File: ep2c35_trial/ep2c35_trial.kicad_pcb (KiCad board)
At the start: 4 copper layers, 70.4 x 57.6 mm, 144 parts, among them J1 Conn_02x21_Odd_Even, J2 Conn_02x21_Odd_Even, J3 3M_8540-4500PL, J4 USB3_B_Micro_Amphenol_GSB343K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, J5 Conn_02x05_Odd_Even, J6 Conn_01x02_Male, J7 Conn_01x02_Male, J8 Conn_01x02_Male, J9 Conn_01x02_Male, U1 EP2C5F484, U2 MIC37302, U3 FT600Q-B-T, U4 W25Q16JVSNIQ, U5 MIC39102, U6 MIC49150-1.2, X1 FNETHE025, Y1 ABM7-30.000MHZ-D2Y-T

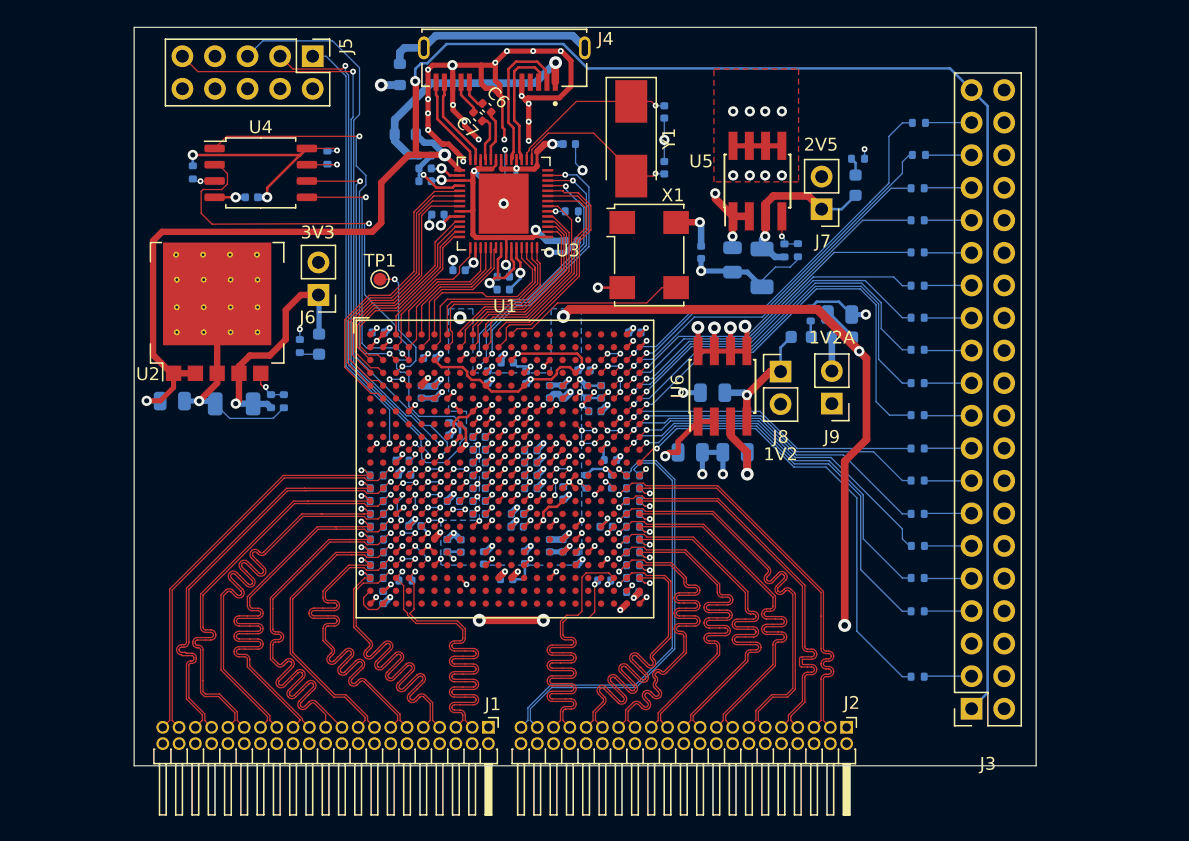
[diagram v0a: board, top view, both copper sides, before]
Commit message: Add lvds_tx.
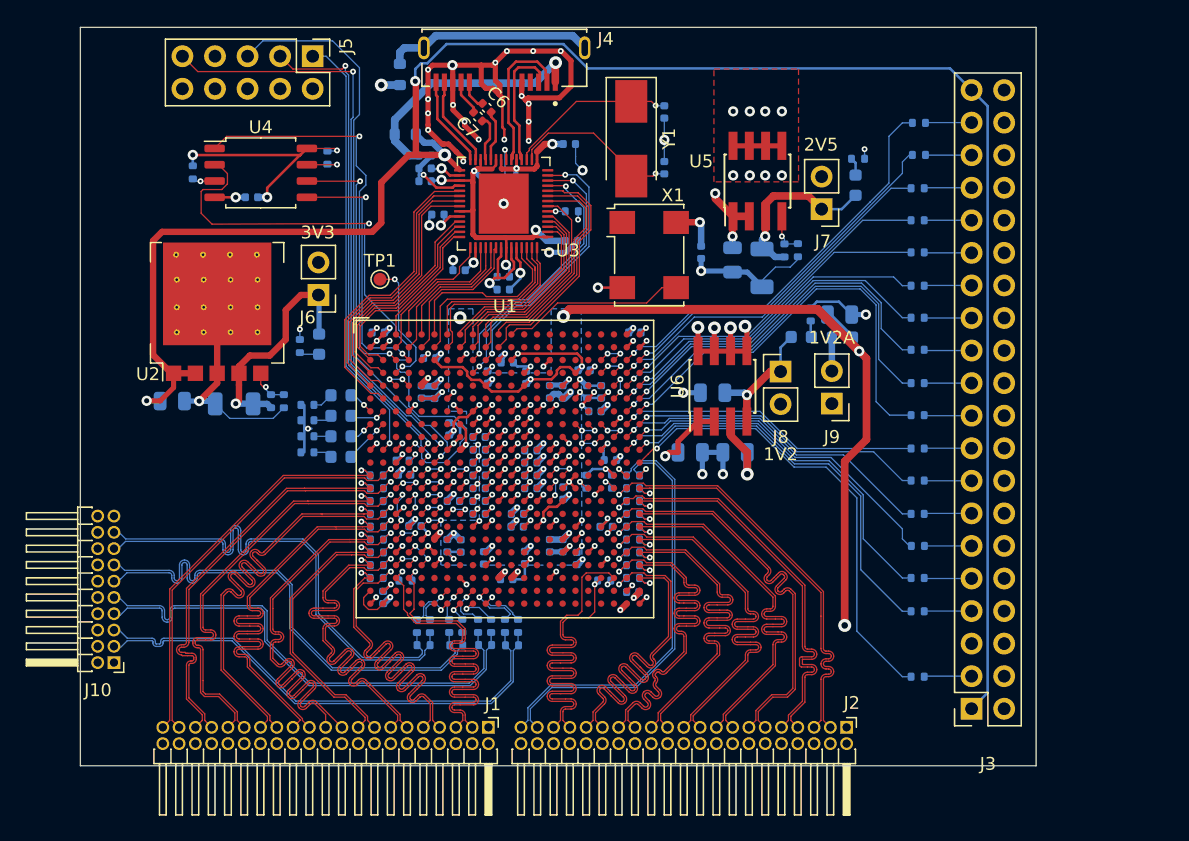
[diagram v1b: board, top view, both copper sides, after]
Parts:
- added D4: LED, LED_SMD:LED_0603_1608Metric, B.Cu at (131.7, 75.8)
- added D5: LED, LED_SMD:LED_0603_1608Metric, B.Cu at (131.7, 77.3)
- added D6: LED, LED_SMD:LED_0603_1608Metric, B.Cu at (131.7, 79.0)
- added D7: LED, LED_SMD:LED_0603_1608Metric, B.Cu at (131.7, 80.5)
- added J10: Conn_02x10_Odd_Even, Connector_PinHeader_1.27mm:PinHeader_2x10_P1.27mm_Horizontal, F.Cu at (114.0, 96.6)
- added R52: 1k, Resistor_SMD:R_0402_1005Metric, B.Cu at (129.1, 76.5)
- added R53: 1k, Resistor_SMD:R_0402_1005Metric, B.Cu at (129.1, 77.7)
- added R54: 1k, Resistor_SMD:R_0402_1005Metric, B.Cu at (129.1, 79.0)
- added R55: 1k, Resistor_SMD:R_0402_1005Metric, B.Cu at (129.1, 80.2)
- added R56: 120, Resistor_SMD:R_0402_1005Metric, B.Cu at (144.5, 93.7)
- added R57: 170, Resistor_SMD:R_0402_1005Metric, B.Cu at (145.1, 95.2)
- added R58: 120, Resistor_SMD:R_0402_1005Metric, B.Cu at (145.5, 93.7)
- added R59: 120, Resistor_SMD:R_0402_1005Metric, B.Cu at (142.4, 93.7)
- added R60: 170, Resistor_SMD:R_0402_1005Metric, B.Cu at (142.9, 95.2)
- added R61: 120, Resistor_SMD:R_0402_1005Metric, B.Cu at (143.4, 93.7)
- added R62: 120, Resistor_SMD:R_0402_1005Metric, B.Cu at (140.2, 93.7)
- added R63: 170, Resistor_SMD:R_0402_1005Metric, B.Cu at (140.7, 95.2)
- added R64: 120, Resistor_SMD:R_0402_1005Metric, B.Cu at (141.2, 93.7)
- added R65: 120, Resistor_SMD:R_0402_1005Metric, B.Cu at (137.6, 93.8)
- added R66: 170, Resistor_SMD:R_0402_1005Metric, B.Cu at (138.2, 95.2)
- added R67: 120, Resistor_SMD:R_0402_1005Metric, B.Cu at (138.7, 93.8)
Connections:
- U1 pad AA10: unconnected-(U1-PadAA10) -> /LVDS_TX_DATA0_RAW_N
- U1 pad AA7: unconnected-(U1-PadAA7) -> /LVDS_TX_DATA3_RAW_N
- U1 pad AA8: unconnected-(U1-PadAA8) -> /LVDS_TX_DATA2_RAW_N
- U1 pad AA9: unconnected-(U1-PadAA9) -> /LVDS_TX_DATA1_RAW_N
- U1 pad AB10: unconnected-(U1-PadAB10) -> /LVDS_TX_DATA0_RAW_P
- U1 pad AB7: unconnected-(U1-PadAB7) -> /LVDS_TX_DATA3_RAW_P
- U1 pad AB8: unconnected-(U1-PadAB8) -> /LVDS_TX_DATA2_RAW_P
- U1 pad AB9: unconnected-(U1-PadAB9) -> /LVDS_TX_DATA1_RAW_P
- U1 pad G1: unconnected-(U1-PadG1) -> /LED0
- U1 pad G2: unconnected-(U1-PadG2) -> /LED1
- U1 pad H1: unconnected-(U1-PadH1) -> /LED2
- U1 pad H2: unconnected-(U1-PadH2) -> /LED3
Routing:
- net /LVDS_TX_DATA0_P: track 0.00 -> 38.7 mm
- net /LVDS_TX_DATA0_N: track 0.00 -> 38.4 mm
- net /LVDS_TX_DATA1_P: track 0.00 -> 38.4 mm
- net /LVDS_TX_DATA2_P: track 0.00 -> 38.3 mm
- net /LVDS_TX_DATA3_P: track 0.00 -> 38.2 mm
- net /LVDS_TX_DATA1_N: track 0.00 -> 38.1 mm
- net /LVDS_TX_DATA3_N: track 0.00 -> 37.9 mm
- net /LVDS_TX_DATA2_N: track 0.00 -> 37.9 mm
- net +1V2A: track 66.1 -> 61.1 mm, vias 10 -> 8
- net /LVDS_TX_DATA0_RAW_N: track 0.00 -> 4.28 mm, vias 0 -> 1
- net GND: track 232.5 -> 236.8 mm, vias 126 -> 127
- net /LVDS_TX_DATA0_RAW_P: track 0.00 -> 4.20 mm, vias 0 -> 1
- net /LVDS_TX_DATA3_RAW_N: track 0.00 -> 3.70 mm, vias 0 -> 1
- net /LVDS_TX_DATA1_RAW_N: track 0.00 -> 3.60 mm, vias 0 -> 1
- net /LED3: track 0.00 -> 3.59 mm, vias 0 -> 1
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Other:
- board size 70.4 x 57.6 mm -> 74.5 x 57.6 mm

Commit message: Top ground plan.
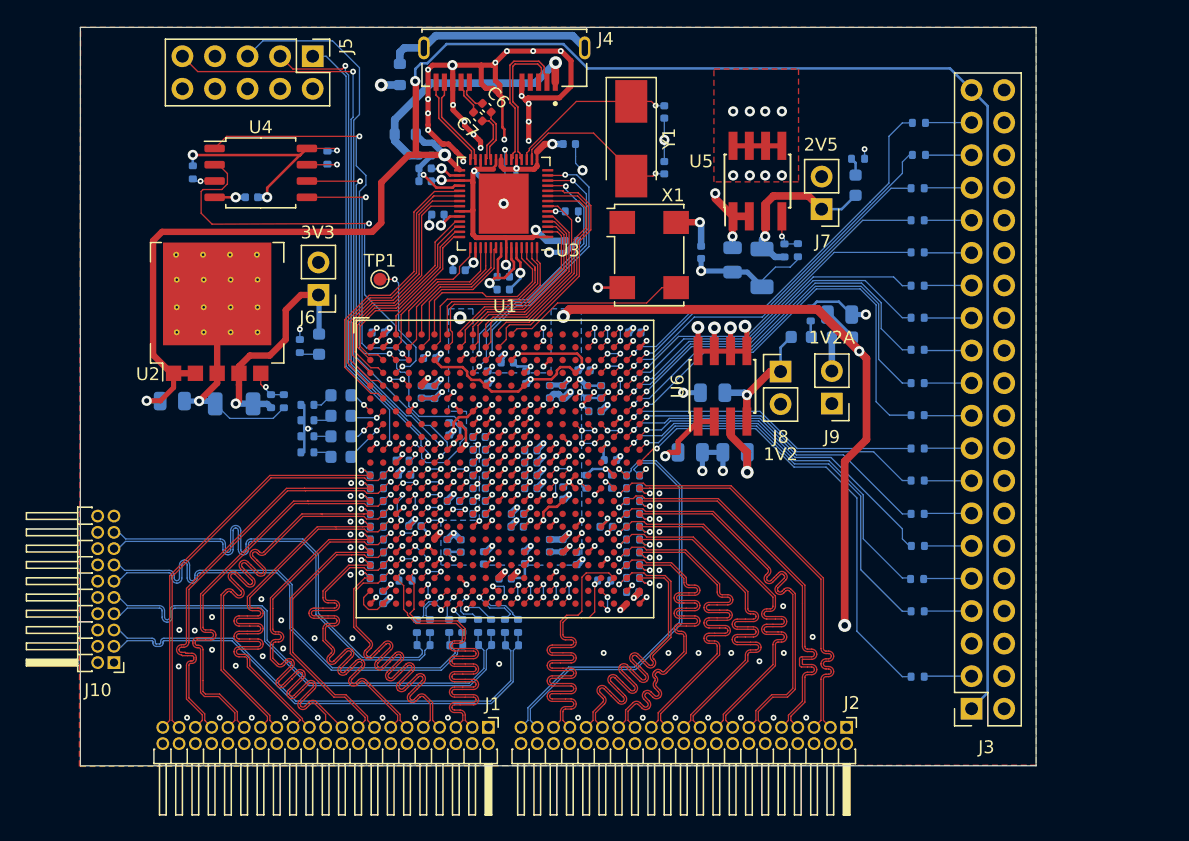
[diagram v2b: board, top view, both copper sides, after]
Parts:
- moved C69 0.12 mm to (144.5, 90.0)
- moved R34 0.09 mm to (176.7, 90.1)
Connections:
- C1 pad 2: GND -> GNDD
- C10 pad 1: GND -> GNDD
- C11 pad 1: GND -> GNDD
- C12 pad 1: GND -> GNDD
- C13 pad 1: GND -> GNDD
- C14 pad 1: GND -> GNDD
- C15 pad 1: GND -> GNDD
- C16 pad 1: GND -> GNDD
- C17 pad 1: GND -> GNDD
- C18 pad 1: GND -> GNDD
- C19 pad 1: GND -> GNDD
- C2 pad 2: GND -> GNDD
- C20 pad 1: GND -> GNDD
- C22 pad 1: GND -> GNDD
- C23 pad 1: GND -> GNDD
- C24 pad 1: GND -> GNDD
- C25 pad 1: GND -> GNDD
- C26 pad 1: GND -> GNDD
- C27 pad 1: GND -> GNDD
- C28 pad 1: GND -> GNDD
- C29 pad 1: GND -> GNDD
- C3 pad 2: GND -> GNDD
- C30 pad 1: GND -> GNDD
- C31 pad 2: GND -> GNDD
- C32 pad 2: GND -> GNDD
- C33 pad 2: GND -> GNDD
- C34 pad 2: GND -> GNDD
- C35 pad 2: GND -> GNDD
- C36 pad 2: GND -> GNDD
- C37 pad 2: GND -> GNDD
- C38 pad 2: GND -> GNDD
- C39 pad 2: GND -> GNDD
- C4 pad 2: GND -> GNDD
- C40 pad 2: GND -> GNDD
- C41 pad 2: GND -> GNDD
- C42 pad 2: GND -> GNDD
- C43 pad 2: GND -> GNDD
- C44 pad 2: GND -> GNDD
- C45 pad 2: GND -> GNDD
- C46 pad 2: GND -> GNDD
- C47 pad 2: GND -> GNDD
- C48 pad 2: GND -> GNDD
- C49 pad 2: GND -> GNDD
- C5 pad 2: GND -> GNDD
- C50 pad 2: GND -> GNDD
- C51 pad 2: GND -> GNDD
- C52 pad 2: GND -> GNDD
- C53 pad 2: GND -> GNDD
- C54 pad 2: GND -> GNDD
- C55 pad 2: GND -> GNDD
- C56 pad 2: GND -> GNDD
- C57 pad 2: GND -> GNDD
- C58 pad 2: GND -> GNDD
- C59 pad 2: GND -> GNDD
- C60 pad 2: GND -> GNDD
- C61 pad 2: GND -> GNDD
- C62 pad 2: GND -> GNDD
- C63 pad 2: GND -> GNDD
- C64 pad 2: GND -> GNDD
- C65 pad 2: GND -> GNDD
- C66 pad 2: GND -> GNDD
- C67 pad 2: GND -> GNDD
- C68 pad 2: GND -> GNDD
- C69 pad 2: GND -> GNDD
- C70 pad 2: GND -> GNDD
- C8 pad 1: GND -> GNDD
- C9 pad 1: GND -> GNDD
- FB2 pad 2: GND -> GNDD
- J1 pad 1: GND -> GNDD
- J1 pad 10: GND -> GNDD
- J1 pad 12: GND -> GNDD
- J1 pad 14: GND -> GNDD
- J1 pad 16: GND -> GNDD
- J1 pad 18: GND -> GNDD
- J1 pad 2: GND -> GNDD
- J1 pad 20: GND -> GNDD
- J1 pad 22: GND -> GNDD
- J1 pad 24: GND -> GNDD
- J1 pad 26: GND -> GNDD
- J1 pad 28: GND -> GNDD
- J1 pad 30: GND -> GNDD
- J1 pad 32: GND -> GNDD
- J1 pad 34: GND -> GNDD
- J1 pad 36: GND -> GNDD
- J1 pad 38: GND -> GNDD
- J1 pad 4: GND -> GNDD
- J1 pad 40: GND -> GNDD
- J1 pad 42: GND -> GNDD
- J1 pad 6: GND -> GNDD
- J1 pad 8: GND -> GNDD
- J10 pad 1: GND -> GNDD
- J10 pad 10: GND -> GNDD
- J10 pad 12: GND -> GNDD
- J10 pad 14: GND -> GNDD
- J10 pad 16: GND -> GNDD
- J10 pad 18: GND -> GNDD
- J10 pad 19: GND -> GNDD
- J10 pad 2: GND -> GNDD
- J10 pad 20: GND -> GNDD
- J10 pad 4: GND -> GNDD
- J10 pad 5: /LVDS_TX_DATA0_N -> GNDD
- J10 pad 6: GND -> GNDD
- J10 pad 8: GND -> GNDD
- J2 pad 1: GND -> GNDD
- J2 pad 10: GND -> GNDD
- J2 pad 12: GND -> GNDD
- J2 pad 14: GND -> GNDD
- J2 pad 16: GND -> GNDD
- J2 pad 18: GND -> GNDD
- J2 pad 2: GND -> GNDD
- J2 pad 20: GND -> GNDD
- J2 pad 22: GND -> GNDD
- J2 pad 24: GND -> GNDD
- J2 pad 26: GND -> GNDD
- J2 pad 28: GND -> GNDD
- J2 pad 30: GND -> GNDD
- J2 pad 32: GND -> GNDD
- J2 pad 34: GND -> GNDD
- J2 pad 36: GND -> GNDD
- J2 pad 38: GND -> GNDD
- J2 pad 4: GND -> GNDD
- J2 pad 40: GND -> GNDD
- J2 pad 42: GND -> GNDD
- J2 pad 6: GND -> GNDD
- J2 pad 8: GND -> GNDD
- J3 pad 10: GND -> GNDD
- J3 pad 12: GND -> GNDD
- J3 pad 14: GND -> GNDD
- J3 pad 16: GND -> GNDD
- J3 pad 18: GND -> GNDD
- J3 pad 2: GND -> GNDD
- J3 pad 20: GND -> GNDD
- J3 pad 22: GND -> GNDD
- J3 pad 24: GND -> GNDD
- J3 pad 26: GND -> GNDD
- J3 pad 28: GND -> GNDD
- J3 pad 30: GND -> GNDD
- J3 pad 32: GND -> GNDD
- J3 pad 34: GND -> GNDD
- J3 pad 36: GND -> GNDD
- J3 pad 38: GND -> GNDD
- J3 pad 4: GND -> GNDD
- J3 pad 40: GND -> GNDD
- J3 pad 6: GND -> GNDD
- J3 pad 8: GND -> GNDD
- J4 pad 5: GND -> GNDD
- J4 pad 8: GND -> GNDD
- J5 pad 10: GND -> GNDD
- J5 pad 2: GND -> GNDD
- R1 pad 2: GND -> GNDD
- R31 pad 1: GND -> GNDD
- R49 pad 1: GND -> GNDD
- R50 pad 1: GND -> GNDD
- R51 pad 1: GND -> GNDD
- R52 pad 1: GND -> GNDD
- R53 pad 1: GND -> GNDD
- R54 pad 1: GND -> GNDD
- R55 pad 1: GND -> GNDD
- R56 pad 1: /LVDS_TX_DATA0_N -> GNDD
- R57 pad 2: /LVDS_TX_DATA0_N -> GNDD
- R9 pad 1: GND -> GNDD
- U1 pad A1: GND -> GNDD
- U1 pad A14: unconnected-(U1-PadA14) -> /LVDS76
- U1 pad A18: unconnected-(U1-PadA18) -> /LVDS96
- U1 pad A19: unconnected-(U1-PadA19) -> /LVDS97
- U1 pad A20: unconnected-(U1-PadA20) -> /LVDS98
- U1 pad A22: GND -> GNDD
- U1 pad AA11: unconnected-(U1-PadAA11) -> /LVDS177
- U1 pad AA12: unconnected-(U1-PadAA12) -> /LVDS176
- U1 pad AA13: unconnected-(U1-PadAA13) -> /LVDS174
- U1 pad AA14: unconnected-(U1-PadAA14) -> /LVDS170
- U1 pad AA15: unconnected-(U1-PadAA15) -> /LVDS169
- U1 pad AA16: unconnected-(U1-PadAA16) -> /LVDS168
- U1 pad AA19: unconnected-(U1-PadAA19) -> /LVDS152
- U1 pad AA2: GND -> GNDD
- U1 pad AA21: GND -> GNDD
- U1 pad AA5: unconnected-(U1-PadAA5) -> /LVDS197
- U1 pad AB1: GND -> GNDD
- U1 pad AB11: unconnected-(U1-PadAB11) -> /LVDS177
- U1 pad AB12: unconnected-(U1-PadAB12) -> /LVDS176
- U1 pad AB13: unconnected-(U1-PadAB13) -> /LVDS174
- U1 pad AB14: unconnected-(U1-PadAB14) -> /LVDS170
- U1 pad AB15: unconnected-(U1-PadAB15) -> /LVDS169
- U1 pad AB16: unconnected-(U1-PadAB16) -> /LVDS168
- U1 pad AB19: unconnected-(U1-PadAB19) -> /LVDS152
- U1 pad AB22: GND -> GNDD
- U1 pad AB5: unconnected-(U1-PadAB5) -> /LVDS197
- U1 pad B14: unconnected-(U1-PadB14) -> /LVDS76
- U1 pad B18: unconnected-(U1-PadB18) -> /LVDS96
- U1 pad B19: unconnected-(U1-PadB19) -> /LVDS97
- U1 pad B2: GND -> GNDD
- U1 pad B20: unconnected-(U1-PadB20) -> /LVDS98
- U1 pad B21: GND -> GNDD
- U1 pad C15: GND -> GNDD
- U1 pad C5: GND -> GNDD
- U1 pad C8: GND -> GNDD
- U1 pad D10: GND -> GNDD
- U1 pad D13: GND -> GNDD
- U1 pad D18: GND -> GNDD
- U1 pad E16: GND -> GNDD
- U1 pad E17: GND -> GNDD
- U1 pad F18: GND -> GNDD
- U1 pad F19: GND -> GNDD
- U1 pad F5: GND -> GNDD
- U1 pad F6: GND -> GNDD
- U1 pad F7: GND -> GNDD
- U1 pad G10: GND -> GNDD
- U1 pad G13: GND -> GNDD
- U1 pad G15: GND -> GNDD
- U1 pad G4: GND -> GNDD
- U1 pad H10: GND -> GNDD
- U1 pad H20: GND -> GNDD
- U1 pad H9: GND -> GNDD
- U1 pad J8: GND -> GNDD
- U1 pad J9: GND -> GNDD
- U1 pad K1: GND -> GNDD
- U1 pad K10: GND -> GNDD
- U1 pad K11: GND -> GNDD
- U1 pad K12: GND -> GNDD
- U1 pad K13: GND -> GNDD
- U1 pad K15: GND -> GNDD
- U1 pad K16: GND -> GNDD
- U1 pad K19: GND -> GNDD
- U1 pad K3: GND -> GNDD
- U1 pad K7: GND -> GNDD
- U1 pad L10: GND -> GNDD
- U1 pad L11: GND -> GNDD
- U1 pad L12: GND -> GNDD
- U1 pad L13: GND -> GNDD
- U1 pad L15: GND -> GNDD
- U1 pad M10: GND -> GNDD
- U1 pad M11: GND -> GNDD
- U1 pad M12: GND -> GNDD
- U1 pad M13: GND -> GNDD
- U1 pad M17: GND -> GNDD
- U1 pad M4: GND -> GNDD
- U1 pad N10: GND -> GNDD
- U1 pad N11: GND -> GNDD
- U1 pad N12: GND -> GNDD
- U1 pad N13: GND -> GNDD
- U1 pad N16: GND -> GNDD
- U1 pad N17: GND -> GNDD
- U1 pad N19: GND -> GNDD
- U1 pad N7: GND -> GNDD
- U1 pad N8: GND -> GNDD
- U1 pad P8: GND -> GNDD
- U1 pad P9: GND -> GNDD
- U1 pad R13: GND -> GNDD
- U1 pad R3: GND -> GNDD
- U1 pad R9: GND -> GNDD
- U1 pad T10: GND -> GNDD
- U1 pad T13: GND -> GNDD
- U1 pad T17: GND -> GNDD
- U1 pad T20: GND -> GNDD
- U1 pad U5: GND -> GNDD
- U1 pad V16: GND -> GNDD
- U1 pad V17: GND -> GNDD
- U1 pad V18: GND -> GNDD
- U1 pad V3: GND -> GNDD
- U1 pad V5: GND -> GNDD
- U1 pad V6: GND -> GNDD
- U1 pad V7: GND -> GNDD
- U1 pad W10: GND -> GNDD
- U1 pad W13: GND -> GNDD
- U1 pad W19: GND -> GNDD
- U1 pad Y15: GND -> GNDD
- U1 pad Y5: unconnected-(U1-PadY5) -> /LVDS198
- U1 pad Y6: unconnected-(U1-PadY6) -> /LVDS198
- U1 pad Y8: GND -> GNDD
- U2 pad 3: GND -> GNDD
- U3 pad 32: GND -> GNDD
- U3 pad 49: GND -> GNDD
- U3 pad 51: GND -> GNDD
- U3 pad 57: GND -> GNDD
- U4 pad 4: GND -> GNDD
- U5 pad 5: GND -> GNDD
- U5 pad 6: GND -> GNDD
- U5 pad 7: GND -> GNDD
- U5 pad 8: GND -> GNDD
- U6 pad 5: GND -> GNDD
- U6 pad 6: GND -> GNDD
- U6 pad 7: GND -> GNDD
- U6 pad 8: GND -> GNDD
- X1 pad 2: GND -> GNDD
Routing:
- net GNDD: track 0.00 -> 275.4 mm, vias 0 -> 183
- net GND: track 236.8 -> 0.00 mm, vias 127 -> 0
- net /LVDS_TX_DATA0_N: track 38.4 -> 0.00 mm
- net /LVDS177: track 0.00 -> 3.04 mm, vias 0 -> 2
- net /LVDS98: track 0.00 -> 2.41 mm, vias 0 -> 2
- net /LVDS97: track 0.00 -> 2.41 mm, vias 0 -> 2
- net /LVDS96: track 0.00 -> 2.41 mm, vias 0 -> 2
- net /LVDS76: track 0.00 -> 2.41 mm, vias 0 -> 2
- net /LVDS198: track 0.00 -> 2.41 mm, vias 0 -> 2
- net /LVDS197: track 0.00 -> 2.41 mm, vias 0 -> 2
- net /LVDS176: track 0.00 -> 2.41 mm, vias 0 -> 2
- net /LVDS174: track 0.00 -> 2.41 mm, vias 0 -> 2
- net /LVDS170: track 0.00 -> 2.41 mm, vias 0 -> 2
- net /LVDS169: track 0.00 -> 2.41 mm, vias 0 -> 2
- net /LVDS168: track 0.00 -> 2.41 mm, vias 0 -> 2
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- added copper zone on F.Cu, net GNDD
- added copper zone on In1.Cu, net GNDD
- removed copper zone on F.Cu, net GND
- removed copper zone on In1.Cu, net GND

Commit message: Add ESD protection.
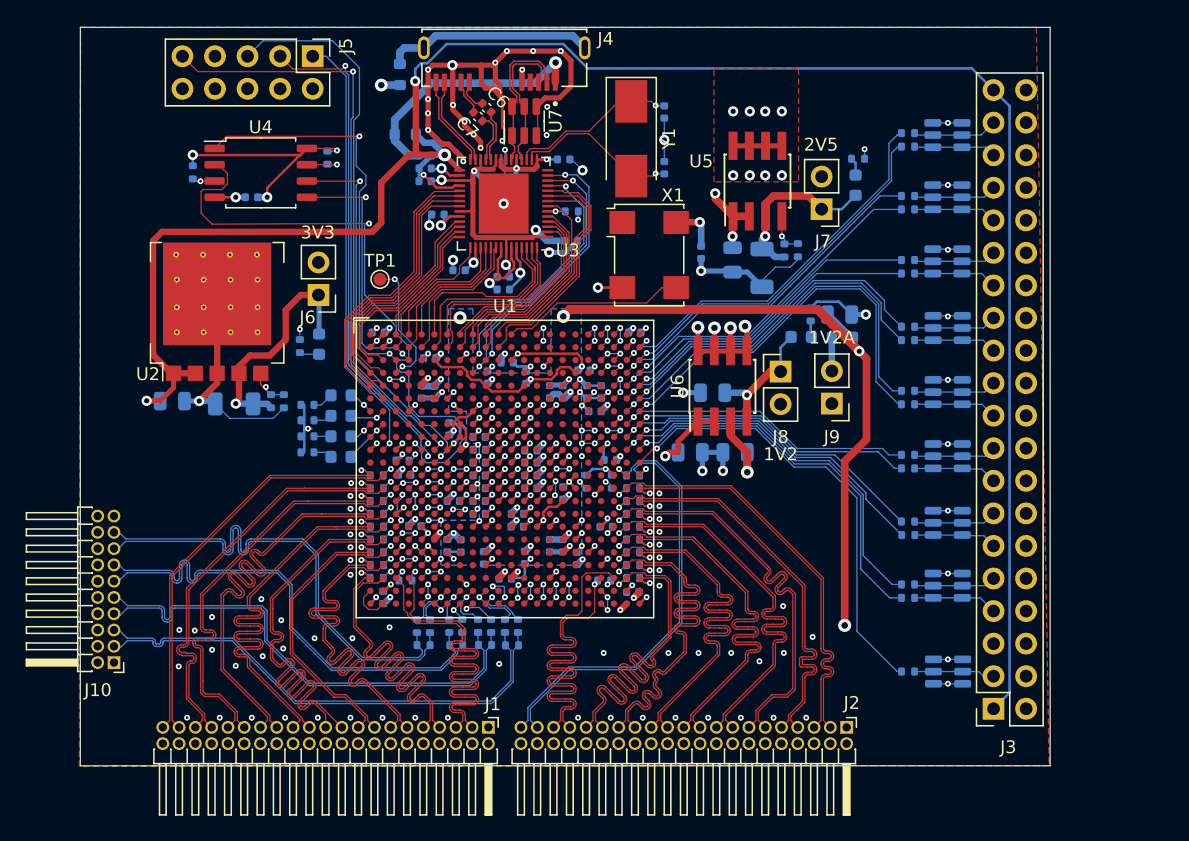
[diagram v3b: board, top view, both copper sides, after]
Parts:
- added U10: SP3003-02UTG, Package_TO_SOT_SMD:SOT-23-6, B.Cu at (179.0, 65.3)
- added U11: SP3003-02UTG, Package_TO_SOT_SMD:SOT-23-6, B.Cu at (179.0, 70.5)
- added U12: SP3003-02UTG, Package_TO_SOT_SMD:SOT-23-6, B.Cu at (179.0, 75.5)
- added U13: SP3003-02UTG, Package_TO_SOT_SMD:SOT-23-6, B.Cu at (179.0, 80.5)
- added U14: SP3003-02UTG, Package_TO_SOT_SMD:SOT-23-6, B.Cu at (179.0, 85.7)
- added U15: SP3003-02UTG, Package_TO_SOT_SMD:SOT-23-6, B.Cu at (179.0, 90.6)
- added U16: SP3003-02UTG, Package_TO_SOT_SMD:SOT-23-6, B.Cu at (179.1, 97.3)
- added U7: SP3003-02UTG, Package_TO_SOT_SMD:SOT-23-6, F.Cu at (146.0, 54.4)
- added U8: SP3003-02UTG, Package_TO_SOT_SMD:SOT-23-6, B.Cu at (179.0, 55.5)
- added U9: SP3003-02UTG, Package_TO_SOT_SMD:SOT-23-6, B.Cu at (179.0, 60.3)
- moved J3 1.71 mm to (182.6, 100.2)
- moved R33 1.29 mm to (175.9, 91.5)
- moved C14 1.28 mm to (149.1, 57.4)
- moved R37 1.21 mm to (175.9, 81.5)
- moved R43 1.21 mm to (175.9, 66.2)
- moved R48 1.17 mm to (175.9, 55.3)
- moved R45 1.13 mm to (175.9, 61.2)
- moved R35 1.13 mm to (176.0, 86.7)
- moved R39 1.13 mm to (175.9, 76.5)
- moved R47 1.07 mm to (175.9, 56.4)
- moved R41 1.06 mm to (175.9, 71.5)
- moved R42 1.03 mm to (175.9, 70.4)
- moved R40 0.96 mm to (175.9, 75.4)
- moved R44 0.96 mm to (175.9, 65.2)
- moved R46 0.96 mm to (175.9, 60.2)
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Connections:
- J10 pad 5: GNDD -> /LVDS_TX_DATA0_N
- R56 pad 1: GNDD -> /LVDS_TX_DATA0_N
- R57 pad 2: GNDD -> /LVDS_TX_DATA0_N
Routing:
- net /LVDS_TX_DATA0_N: track 0.00 -> 38.4 mm
- net GNDD: track 275.4 -> 256.5 mm, vias 183 -> 192
- net /POD_D15: track 3.71 -> 6.59 mm
- net /POD_D11: track 3.71 -> 6.56 mm
- net /POD_D6: track 3.68 -> 6.52 mm
- net /POD_D5: track 3.71 -> 6.55 mm
- net /POD_D13: track 3.68 -> 6.52 mm
- net /POD_D9: track 3.72 -> 6.53 mm
- net /POD_D3: track 3.70 -> 6.51 mm
- net /POD_D12: track 3.72 -> 6.51 mm
- net /POD_D2: track 3.72 -> 6.51 mm
- net /POD_D8: track 3.70 -> 6.49 mm
- net /POD_D0: track 3.61 -> 6.39 mm
- net /POD_D14: track 3.66 -> 6.43 mm
- net /POD_D7: track 3.72 -> 6.50 mm
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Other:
- board size 74.5 x 57.6 mm -> 75.6 x 57.6 mm
